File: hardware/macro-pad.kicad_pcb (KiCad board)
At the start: 2 copper layers, 94 x 71 mm, 43 parts, among them J1 USB_C_Receptacle_USB2.0, SW1 PEC12R-4025F-S0024, SW2 MX1A-G1NA, SW3 MX1A-G1NA, SW4 MX1A-G1NA, SW5 MX1A-G1NA, U1 MIC5317-3.3ZD5-TR, U2 RP2040, U3 W25Q128JVSIQ, Y1 ABLS-12.000MHZ-B4-T

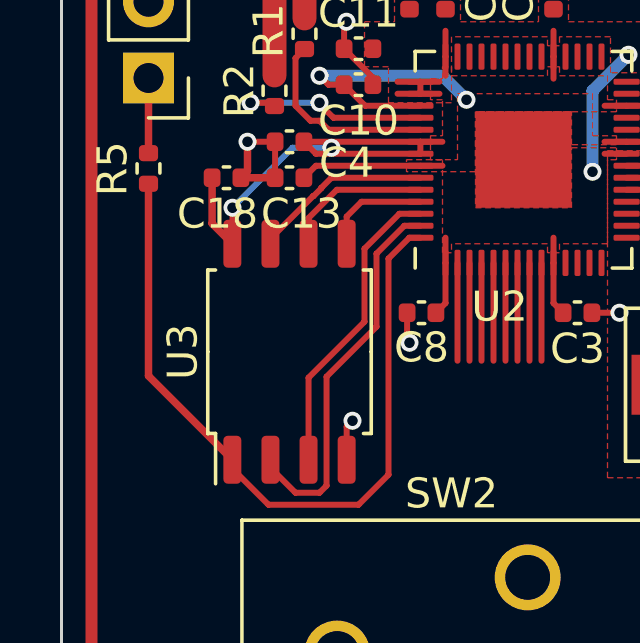
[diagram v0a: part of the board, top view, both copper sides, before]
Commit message: Rearranged micocontroller pins for easier routing
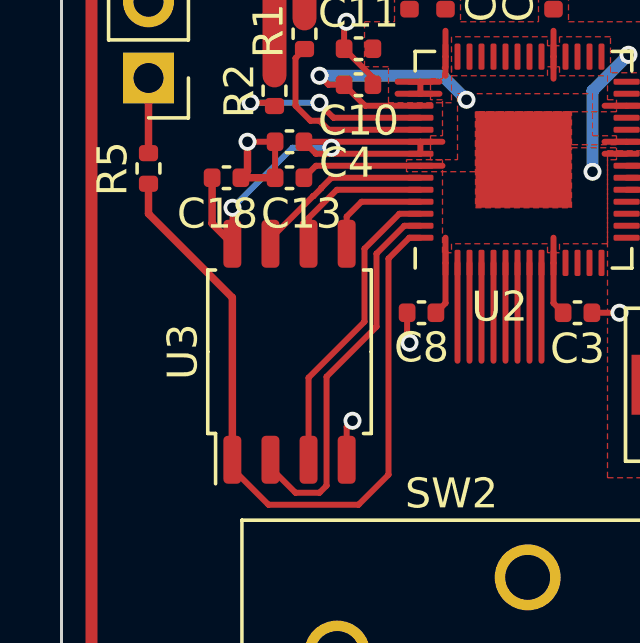
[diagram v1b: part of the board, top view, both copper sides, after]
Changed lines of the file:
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@@
       (rotate (xyz 0 0 0))
+    )
+    (model "${KIPRJMOD}/lib/kaith_switch.step"
+      (offset (xyz -2.5 -5 5))
+      (scale (xyz 1 1 1))
+      (rotate (xyz 0 0 -90))
     )
   )
@@
       (rotate (xyz 0 0 0))
     )
+    (model "${KIPRJMOD}/lib/kaith_switch.step"
+      (offset (xyz -2.5 -5 5))
+      (scale (xyz 1 1 1))
+      (rotate (xyz 0 0 -90))
+    )
   )
   (footprint "Resistor_SMD:R_0402_1005Metric" (layer "F.Cu")
@@
       (scale (xyz 1 1 1))
       (rotate (xyz 0 0 0))
+    )
+    (model "${KIPRJMOD}/lib/kaith_switch.step"
+      (offset (xyz -2.5 -5 5))
+      (scale (xyz 1 1 1))
+      (rotate (xyz 0 0 -90))
     )
   )
@@
   (segment (start 119.69 91.2) (end 115.8375 91.2) (width 0.2) (layer "F.Cu") (net 16))
   (segment (start 102.695 101.295) (end 102.695 101) (width 0.2) (layer "F.Cu") (net 17))
-  (segment (start 99.9 98.205) (end 102.695 101) (width 0.25) (layer "F.Cu") (net 17))
+  (segment (start 102.695 95.595) (end 102.695 101) (width 0.25) (layer "F.Cu") (net 17))
   (segment (start 103.9 102.5) (end 102.695 101.295) (width 0.2) (layer "F.Cu") (net 17))
   (segment (start 108.595711 93.6) (end 107.9 94.295711) (width 0.2) (layer "F.Cu") (net 17))
+  (segment (start 99.9 92.8) (end 102.695 95.595) (width 0.25) (layer "F.Cu") (net 17))
   (segment (start 107.9 101.5) (end 106.9 102.5) (width 0.2) (layer "F.Cu") (net 17))
-  (segment (start 99.9 91.8) (end 99.9 98.205) (width 0.25) (layer "F.Cu") (net 17))
   (segment (start 108.9625 93.6) (end 108.595711 93.6) (width 0.2) (layer "F.Cu") (net 17))
+  (segment (start 99.9 91.8) (end 99.9 92.8) (width 0.25) (layer "F.Cu") (net 17))
   (segment (start 106.9 102.5) (end 103.9 102.5) (width 0.2) (layer "F.Cu") (net 17))
   (segment (start 107.9 94.295711) (end 107.9 101.5) (width 0.2) (layer "F.Cu") (net 17))

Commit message: PCB components have been routed
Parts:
- moved SW4 20.0 mm to (112.5, 124.9)
- moved SW5 20.0 mm to (132.5, 124.9)
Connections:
- U2 pad 2: /D_{LED} -> /SW_{3}
- U2 pad 3: /SW_{1} -> /D_{LED}
- U2 pad 4: /SW_{2} -> /SW_{1}
- U2 pad 5: /SW_{3} -> /SW_{4}
- U2 pad 6: /SW_{4} -> /SW_{2}
- U2 pad 7: /R_{A} -> /R_{BTN}
- U2 pad 8: /R_{B} -> /R_{A}
- U2 pad 9: /R_{BTN} -> /R_{B}
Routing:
- net /R_{A}: track 3.26 -> 57.4 mm
- net /R_{B}: track 3.26 -> 53.5 mm
- net /R_{BTN}: track 3.26 -> 51.6 mm
- net /SW_{4}: track 3.26 -> 40.8 mm, vias 0 -> 1
- net /SW_{3}: track 3.26 -> 37.6 mm
- net /D_{LED}: track 9.61 -> 32.6 mm
- net /SW_{2}: track 3.26 -> 23.6 mm
- net /SW_{1}: track 3.26 -> 15.0 mm
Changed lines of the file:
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@@
       (net 3 "+3V3") (pinfunction "IOVDD") (pintype "power_in"))
     (pad "2" smd roundrect locked (at -3.4375 -2.2 90) (size 0.875 0.2) (layers "F.Cu" "F.Paste" "F.Mask") (roundrect_rratio 0.25)
-      (net 8 "/D_{LED}") (pinfunction "GPIO0") (pintype "bidirectional"))
+      (net 23 "/SW_{3}") (pinfunction "GPIO0") (pintype "bidirectional"))
     (pad "3" smd roundrect locked (at -3.4375 -1.8 90) (size 0.875 0.2) (layers "F.Cu" "F.Paste" "F.Mask") (roundrect_rratio 0.25)
-      (net 21 "/SW_{1}") (pinfunction "GPIO1") (pintype "bidirectional"))
+      (net 8 "/D_{LED}") (pinfunction "GPIO1") (pintype "bidirectional"))
     (pad "4" smd roundrect locked (at -3.4375 -1.4 90) (size 0.875 0.2) (layers "F.Cu" "F.Paste" "F.Mask") (roundrect_rratio 0.25)
-      (net 22 "/SW_{2}") (pinfunction "GPIO2") (pintype "bidirectional"))
+      (net 21 "/SW_{1}") (pinfunction "GPIO2") (pintype "bidirectional"))
     (pad "5" smd roundrect locked (at -3.4375 -1 90) (size 0.875 0.2) (layers "F.Cu" "F.Paste" "F.Mask") (roundrect_rratio 0.25)
-      (net 23 "/SW_{3}") (pinfunction "GPIO3") (pintype "bidirectional"))
+      (net 24 "/SW_{4}") (pinfunction "GPIO3") (pintype "bidirectional"))
     (pad "6" smd roundrect locked (at -3.4375 -0.6 90) (size 0.875 0.2) (layers "F.Cu" "F.Paste" "F.Mask") (roundrect_rratio 0.25)
-      (net 24 "/SW_{4}") (pinfunction "GPIO4") (pintype "bidirectional"))
+      (net 22 "/SW_{2}") (pinfunction "GPIO4") (pintype "bidirectional"))
     (pad "7" smd roundrect locked (at -3.4375 -0.2 90) (size 0.875 0.2) (layers "F.Cu" "F.Paste" "F.Mask") (roundrect_rratio 0.25)
-      (net 18 "/R_{A}") (pinfunction "GPIO5") (pintype "bidirectional"))
+      (net 20 "/R_{BTN}") (pinfunction "GPIO5") (pintype "bidirectional"))
     (pad "8" smd roundrect locked (at -3.4375 0.2 90) (size 0.875 0.2) (layers "F.Cu" "F.Paste" "F.Mask") (roundrect_rratio 0.25)
-      (net 19 "/R_{B}") (pinfunction "GPIO6") (pintype "bidirectional"))
+      (net 18 "/R_{A}") (pinfunction "GPIO6") (pintype "bidirectional"))
     (pad "9" smd roundrect locked (at -3.4375 0.6 90) (size 0.875 0.2) (layers "F.Cu" "F.Paste" "F.Mask") (roundrect_rratio 0.25)
-      (net 20 "/R_{BTN}") (pinfunction "GPIO7") (pintype "bidirectional"))
+      (net 19 "/R_{B}") (pinfunction "GPIO7") (pintype "bidirectional"))
     (pad "10" smd roundrect locked (at -3.4375 1 90) (size 0.875 0.2) (layers "F.Cu" "F.Paste" "F.Mask") (roundrect_rratio 0.25)
       (net 3 "+3V3") (pinfunction "IOVDD") (pintype "passive"))
@@
   )
   (footprint "Button_Switch_Keyboard:SW_Cherry_MX_1.00u_PCB" (layer "F.Cu")
-    (at 132.54 124.92)
+    (at 112.54 124.92)
     (descr "Cherry MX keyswitch, 1.00u, PCB mount, http://cherryamericas.com/wp-content/uploads/2014/12/mx_cat.pdf")
     (tags "Cherry MX keyswitch 1.00u PCB")
@@
   )
   (footprint "Button_Switch_Keyboard:SW_Cherry_MX_1.00u_PCB" (layer "F.Cu")
-    (at 112.54 124.92)
+    (at 132.54 124.92)
     (descr "Cherry MX keyswitch, 1.00u, PCB mount, http://cherryamericas.com/wp-content/uploads/2014/12/mx_cat.pdf")
     (tags "Cherry MX keyswitch 1.00u PCB")
@@
   (segment (start 108.975 114.025) (end 106.99 116.01) (width 0.25) (layer "F.Cu") (net 8))
   (segment (start 110.025 114.025) (end 108.975 114.025) (width 0.25) (layer "F.Cu") (net 8))
-  (segment (start 110.2 94.4375) (end 110.2 97.7) (width 0.2) (layer "F.Cu") (net 8))
   (segment (start 110.45 114.45) (end 110.025 114.025) (width 0.25) (layer "F.Cu") (net 8))
   (segment (start 106.99 116.01) (end 106.99 117.75) (width 0.25) (layer "F.Cu") (net 8))
+  (segment (start 103.125886 107.405485) (end 103.125886 112.145886) (width 0.2) (layer "F.Cu") (net 8))
+  (segment (start 110.6 94.4375) (end 110.6 99.931371) (width 0.2) (layer "F.Cu") (net 8))
   (segment (start 110.45 114.6) (end 110.45 114.45) (width 0.25) (layer "F.Cu") (net 8))
+  (segment (start 110.6 99.931371) (end 103.125886 107.405485) (width 0.2) (layer "F.Cu") (net 8))
+  (segment (start 103.125886 112.145886) (end 106.99 116.01) (width 0.2) (layer "F.Cu") (net 8))
   (segment (start 104.25 79.42) (end 104.25 80.55) (width 0.3) (layer "F.Cu") (net 10))
   (segment (start 105.25 78.545) (end 105.105 78.4) (width 0.3) (layer "F.Cu") (net 10))
@@
   (segment (start 106.9 102.5) (end 103.9 102.5) (width 0.2) (layer "F.Cu") (net 17))
   (segment (start 107.9 94.295711) (end 107.9 101.5) (width 0.2) (layer "F.Cu") (net 17))
-  (segment (start 112.2 94.4375) (end 112.2 97.7) (width 0.2) (layer "F.Cu") (net 18))
-  (segment (start 112.6 94.4375) (end 112.6 97.7) (width 0.2) (layer "F.Cu") (net 19))
-  (segment (start 113 94.4375) (end 113 97.7) (width 0.2) (layer "F.Cu") (net 20))
-  (segment (start 110.6 94.4375) (end 110.6 97.7) (width 0.2) (layer "F.Cu") (net 21))
-  (segment (start 111 94.4375) (end 111 97.7) (width 0.2) (layer "F.Cu") (net 22))
-  (segment (start 111.4 94.4375) (end 111.4 97.7) (width 0.2) (layer "F.Cu") (net 23))
-  (segment (start 111.8 94.4375) (end 111.8 97.7) (width 0.2) (layer "F.Cu") (net 24))
+  (segment (start 112.6 94.4375) (end 112.6 100.602942) (width 0.2) (layer "F.Cu") (net 18))
+  (segment (start 135.009267 99.325047) (end 135.009267 90.7) (width 0.2) (layer "F.Cu") (net 18))
+  (segment (start 117.097058 105.1) (end 129.234314 105.1) (width 0.2) (layer "F.Cu") (net 18))
+  (segment (start 135.009267 90.7) (end 126.809267 82.5) (width 0.2) (layer "F.Cu") (net 18))
+  (segment (start 112.6 100.602942) (end 117.097058 105.1) (width 0.2) (layer "F.Cu") (net 18))
+  (segment (start 126.809267 82.5) (end 122.5 82.5) (width 0.2) (layer "F.Cu") (net 18))
+  (segment (start 129.234314 105.1) (end 135.009267 99.325047) (width 0.2) (layer "F.Cu") (net 18))
+  (segment (start 113 100.437256) (end 117.262744 104.7) (width 0.2) (layer "F.Cu") (net 19))
+  (segment (start 134.609267 99.159361) (end 134.609267 90.865686) (width 0.2) (layer "F.Cu") (net 19))
+  (segment (start 117.262744 104.7) (end 129.068628 104.7) (width 0.2) (layer "F.Cu") (net 19))
+  (segment (start 134.609267 90.865686) (end 131.243581 87.5) (width 0.2) (layer "F.Cu") (net 19))
+  (segment (start 129.068628 104.7) (end 134.609267 99.159361) (width 0.2) (layer "F.Cu") (net 19))
+  (segment (start 113 94.4375) (end 113 100.437256) (width 0.2) (layer "F.Cu") (net 19))
+  (segment (start 131.243581 87.5) (end 122.5 87.5) (width 0.2) (layer "F.Cu") (net 19))
+  (segment (start 135.409267 84.090733) (end 137 82.5) (width 0.2) (layer "F.Cu") (net 20))
+  (segment (start 135.409267 99.490733) (end 135.409267 84.090733) (width 0.2) (layer "F.Cu") (net 20))
+  (segment (start 112.2 94.4375) (end 112.2 100.768628) (width 0.2) (layer "F.Cu") (net 20))
+  (segment (start 112.2 100.768628) (end 116.931372 105.5) (width 0.2) (layer "F.Cu") (net 20))
+  (segment (start 129.4 105.5) (end 135.409267 99.490733) (width 0.2) (layer "F.Cu") (net 20))
+  (segment (start 116.931372 105.5) (end 129.4 105.5) (width 0.2) (layer "F.Cu") (net 20))
+  (segment (start 111 94.4375) (end 111 102.65) (width 0.2) (layer "F.Cu") (net 21))
+  (segment (start 111 102.65) (end 106.19 107.46) (width 0.2) (layer "F.Cu") (net 21))
+  (segment (start 111.8 100.934314) (end 118.325686 107.46) (width 0.2) (layer "F.Cu") (net 22))
+  (segment (start 111.8 94.4375) (end 111.8 100.934314) (width 0.2) (layer "F.Cu") (net 22))
+  (segment (start 118.325686 107.46) (end 126.19 107.46) (width 0.2) (layer "F.Cu") (net 22))
+  (segment (start 102.725886 107.239799) (end 102.725886 123.995886) (width 0.2) (layer "F.Cu") (net 23))
+  (segment (start 102.725886 123.995886) (end 106.19 127.46) (width 0.2) (layer "F.Cu") (net 23))
+  (segment (start 110.2 99.765685) (end 102.725886 107.239799) (width 0.2) (layer "F.Cu") (net 23))
+  (segment (start 110.2 94.4375) (end 110.2 99.765685) (width 0.2) (layer "F.Cu") (net 23))
+  (segment (start 123.4255 113.1255) (end 126.2 113.1255) (width 0.2) (layer "F.Cu") (net 24))
+  (segment (start 111.4 94.4375) (end 111.4 101.1) (width 0.2) (layer "F.Cu") (net 24))
+  (segment (start 111.4 101.1) (end 123.4255 113.1255) (width 0.2) (layer "F.Cu") (net 24))
+  (via (at 126.2 113.1255) (size 0.6) (drill 0.35) (layers "F.Cu" "B.Cu") (net 24))
+  (segment (start 126.2 113.1255) (end 126.19 113.1355) (width 0.2) (layer "B.Cu") (net 24))
+  (segment (start 126.19 113.1355) (end 126.19 127.46) (width 0.2) (layer "B.Cu") (net 24))
   (segment (start 105.402254 92.21) (end 105.66 91.952254) (width 0.2) (layer "F.Cu") (net 50))
   (segment (start 105.66 91.938604) (end 105.998604 91.6) (width 0.2) (layer "F.Cu") (net 50))
